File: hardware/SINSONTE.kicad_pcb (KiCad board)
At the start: 2 copper layers, 90 x 70 mm, 39 parts, among them J1 BAT, J10 Conn_01x01_Male, J11 Conn_01x01_Male, J12 Conn_01x04_Male, J13 Conn_01x01_Male, J14 Conn_01x02_Male, J2 CLOCK, J3 LIGHT_SENSOR, J4 Conn_01x20_Male, J5 Conn_01x01_Male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

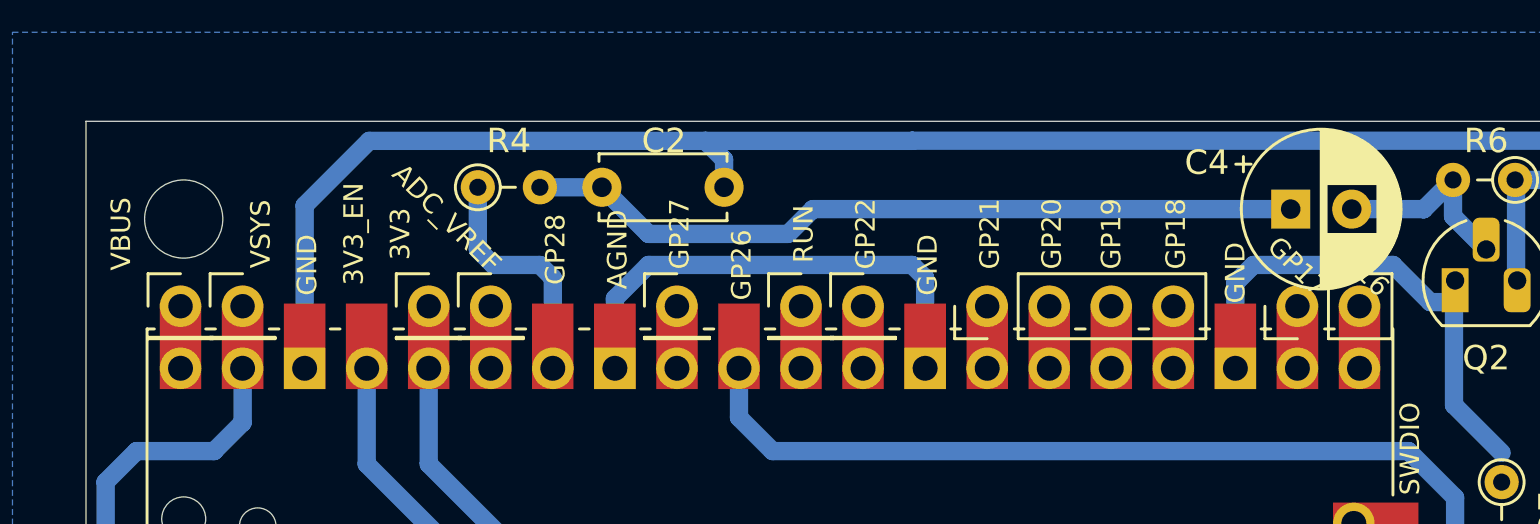
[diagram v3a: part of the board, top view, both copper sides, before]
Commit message: rpi second half conn aded all pins connector
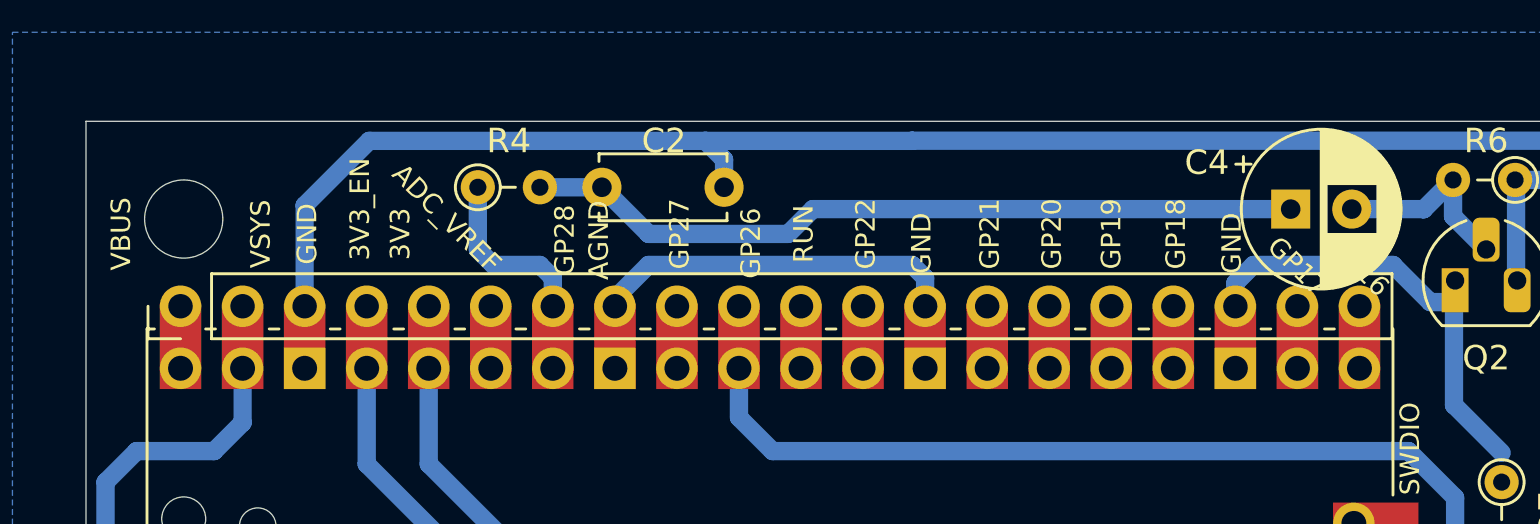
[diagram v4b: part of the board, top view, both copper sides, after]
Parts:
- removed J10, J11, J13, J6, J7, J8: Conn_01x01_Male, Connector_PinHeader_2.54mm:PinHeader_1x01_P2.54mm_Vertical
- removed J12: Conn_01x04_Male, Connector_PinHeader_2.54mm:PinHeader_1x04_P2.54mm_Vertical
- removed J14: Conn_01x02_Male, Connector_PinHeader_2.54mm:PinHeader_1x02_P2.54mm_Vertical
- J5: value Conn_01x01_Male -> Conn_01x20_Male; footprint Connector_PinHeader_2.54mm:PinHeader_1x01_P2.54mm_Vertical -> Connector_PinHeader_2.54mm:PinHeader_1x20_P2.54mm_Vertical
- moved J5 2.54 mm to (53.9, 57.6), turned to 90 degrees
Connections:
- J5 pad 1: Net-(BT1-Pad1) -> Net-(J5-Pad1)
- Q1 pad 3: Net-(Q1-Pad3) -> Net-(J5-Pad4)
- R4 pad 1: Net-(R4-Pad1) -> Net-(J5-Pad7)
- U1 pad 21: Net-(J14-Pad2) -> Net-(J5-Pad20)
- U1 pad 22: Net-(J14-Pad1) -> Net-(J5-Pad19)
- U1 pad 24: Net-(J12-Pad4) -> Net-(J5-Pad17)
- U1 pad 25: Net-(J12-Pad3) -> Net-(J5-Pad16)
- U1 pad 26: Net-(J12-Pad2) -> Net-(J5-Pad15)
- U1 pad 27: Net-(J12-Pad1) -> Net-(J5-Pad14)
- U1 pad 29: Net-(J11-Pad1) -> Net-(J5-Pad12)
- U1 pad 30: Net-(J8-Pad1) -> Net-(J5-Pad11)
- U1 pad 32: Net-(J7-Pad1) -> Net-(J5-Pad9)
- U1 pad 34: Net-(R4-Pad1) -> Net-(J5-Pad7)
- U1 pad 35: Net-(J10-Pad1) -> Net-(J5-Pad6)
- U1 pad 37: Net-(Q1-Pad3) -> Net-(J5-Pad4)
- U1 pad 40: Net-(J13-Pad1) -> Net-(J5-Pad1)
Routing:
- net Net-(J5-Pad4): track 0.00 -> 129.9 mm
- net Net-(Q1-Pad3): track 127.4 -> 0.00 mm
- net Net-(R4-Pad1): track 9.80 -> 0.00 mm
- net Net-(J5-Pad7): track 0.00 -> 9.80 mm
- net Net-(J8-Pad1): track 2.54 -> 0.00 mm
- net Net-(J7-Pad1): track 2.54 -> 0.00 mm
- net Net-(J5-Pad9): track 0.00 -> 2.54 mm
- net Net-(J5-Pad6): track 0.00 -> 2.54 mm
- net Net-(J5-Pad20): track 0.00 -> 2.54 mm
- net Net-(J5-Pad19): track 0.00 -> 2.54 mm
- net Net-(J5-Pad17): track 0.00 -> 2.54 mm
- net Net-(J5-Pad16): track 0.00 -> 2.54 mm
- net Net-(J5-Pad15): track 0.00 -> 2.54 mm
- net Net-(J5-Pad14): track 0.00 -> 2.54 mm
- net Net-(J5-Pad12): track 0.00 -> 2.54 mm
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
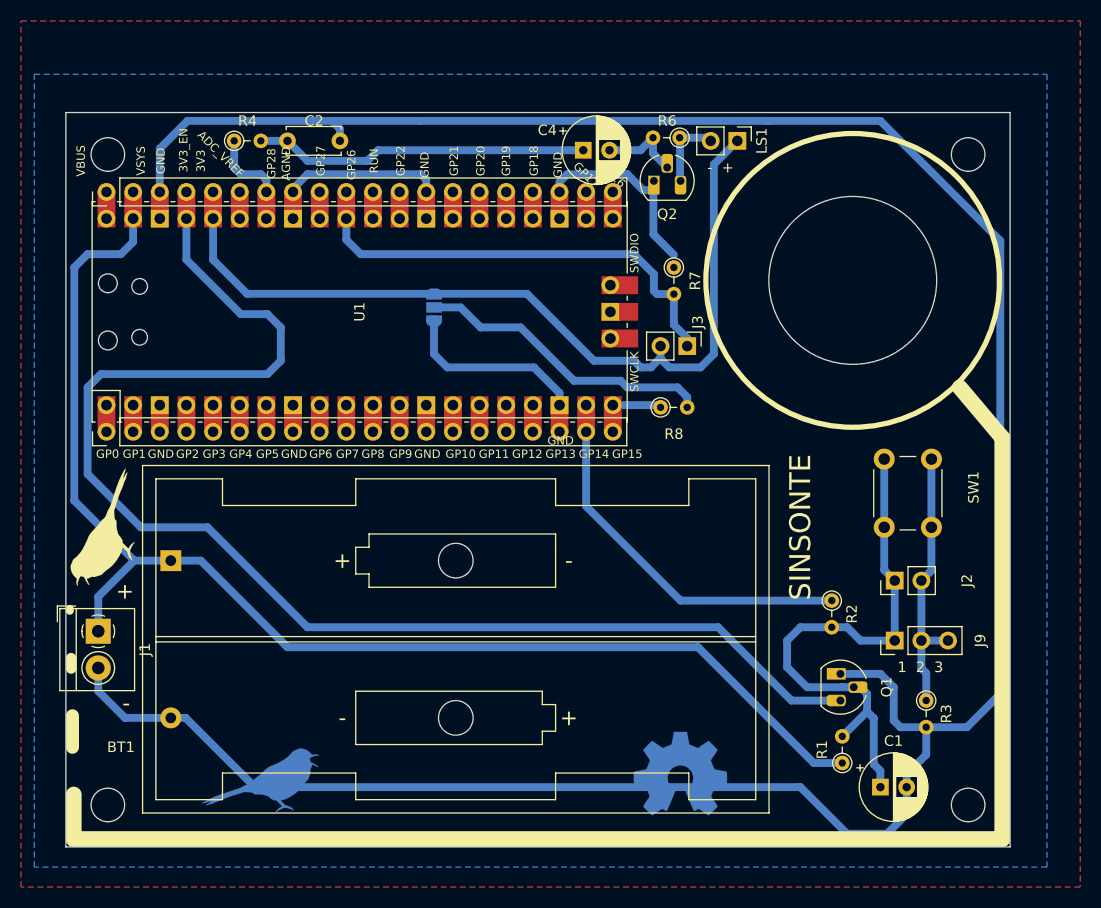
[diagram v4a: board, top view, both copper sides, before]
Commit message: added proto area
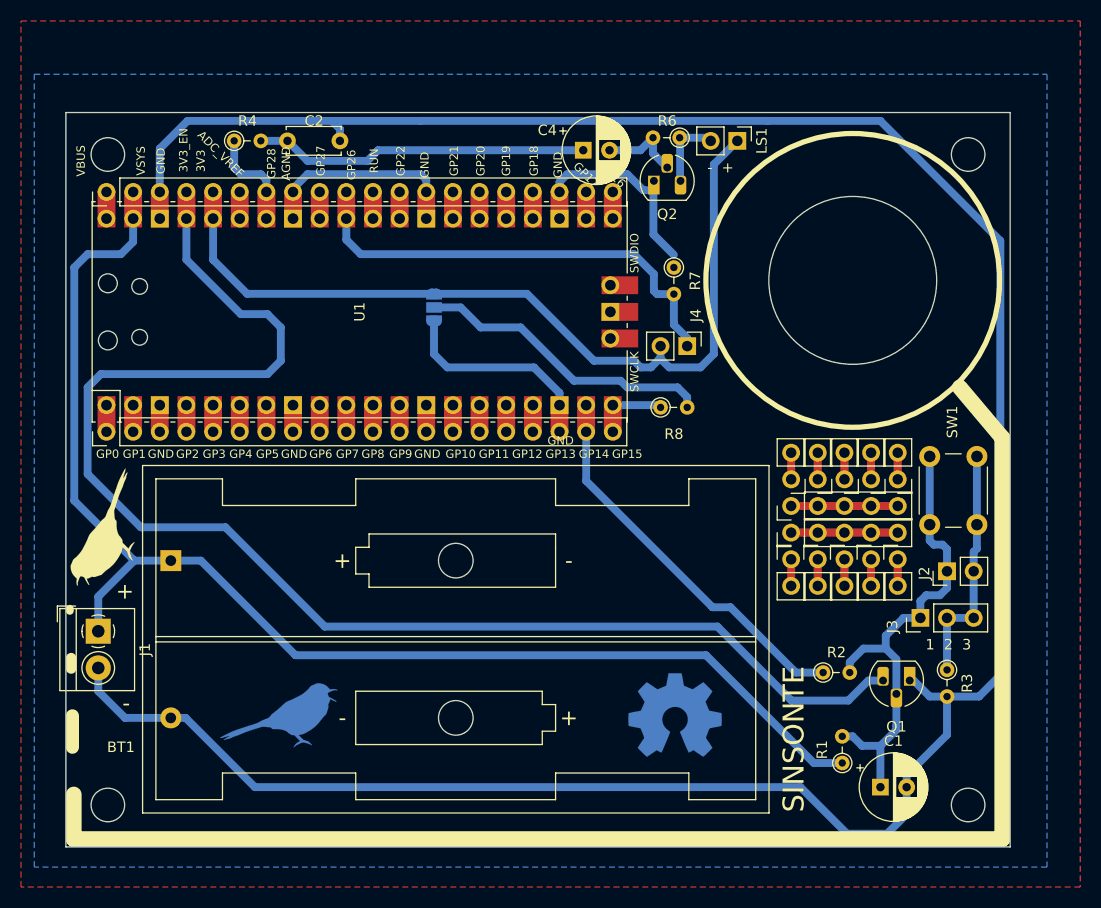
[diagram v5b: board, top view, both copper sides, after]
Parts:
- added J10: Conn_01x02_Male, Connector_PinHeader_2.54mm:PinHeader_1x02_P2.54mm_Vertical, F.Cu at (126.7, 92.6)
- added J11: Conn_01x02_Male, Connector_PinHeader_2.54mm:PinHeader_1x02_P2.54mm_Vertical, F.Cu at (124.2, 92.6)
- added J12: Conn_01x02_Male, Connector_PinHeader_2.54mm:PinHeader_1x02_P2.54mm_Vertical, F.Cu at (121.7, 92.6)
- added J13: Conn_01x02_Male, Connector_PinHeader_2.54mm:PinHeader_1x02_P2.54mm_Vertical, F.Cu at (119.1, 92.6)
- added J14: Conn_01x02_Male, Connector_PinHeader_2.54mm:PinHeader_1x02_P2.54mm_Vertical, F.Cu at (129.3, 85.0)
- added J15: Conn_01x02_Male, Connector_PinHeader_2.54mm:PinHeader_1x02_P2.54mm_Vertical, F.Cu at (126.7, 85.0)
- added J16: Conn_01x02_Male, Connector_PinHeader_2.54mm:PinHeader_1x02_P2.54mm_Vertical, F.Cu at (124.2, 85.0)
- added J17: Conn_01x02_Male, Connector_PinHeader_2.54mm:PinHeader_1x02_P2.54mm_Vertical, F.Cu at (121.7, 85.0)
- added J18: Conn_01x02_Male, Connector_PinHeader_2.54mm:PinHeader_1x02_P2.54mm_Vertical, F.Cu at (119.1, 85.0)
- added J7: Conn_01x05_Male, Connector_PinHeader_2.54mm:PinHeader_1x05_P2.54mm_Vertical, F.Cu at (119.1, 90.0)
- added J8: Conn_01x05_Male, Connector_PinHeader_2.54mm:PinHeader_1x05_P2.54mm_Vertical, F.Cu at (119.1, 87.5)
- added J9: Conn_01x02_Male, Connector_PinHeader_2.54mm:PinHeader_1x02_P2.54mm_Vertical, F.Cu at (129.3, 92.6)
- moved R2 6.91 mm to (122.2, 103.4), turned to 0 degrees
- moved Q1 6.63 mm to (130.4, 104.1), turned to 180 degrees
- moved G*** 6.45 mm to (70.3, 107.4)
- moved REF** 5.61 mm to (108.1, 107.4)
- moved J2 5.06 mm to (134.0, 93.7)
- moved SW1 4.34 mm to (132.3, 89.3)
- moved R3 3.53 mm to (134.0, 103.1)
- moved J3 3.26 mm to (131.4, 98.2)
- moved G*** 2.33 mm to (112.9, 79.5)
- renumbered J9 to J3, J3 to J4, J4 to J5, J5 to J6
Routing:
- net Net-(J8-Pad1): track 0.00 -> 20.3 mm
- net Net-(J7-Pad1): track 0.00 -> 20.3 mm
- net Net-(BT1-Pad2): track 323.3 -> 315.0 mm
- net Net-(C1-Pad1): track 53.0 -> 46.8 mm
- net Net-(J9-Pad1): track 0.00 -> 5.08 mm
- net Net-(J13-Pad1): track 0.00 -> 5.08 mm
- net Net-(J12-Pad1): track 0.00 -> 5.08 mm
- net Net-(J11-Pad1): track 0.00 -> 5.08 mm
- net Net-(J10-Pad1): track 0.00 -> 5.08 mm
- net Net-(J18-Pad1): track 0.00 -> 5.08 mm
- net Net-(J17-Pad1): track 0.00 -> 5.08 mm
- net Net-(J16-Pad1): track 0.00 -> 5.08 mm
- net Net-(J15-Pad1): track 0.00 -> 5.08 mm
- net Net-(J14-Pad1): track 0.00 -> 5.08 mm
- net Net-(J6-Pad4): track 129.9 -> 134.6 mm
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
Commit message: minor adjustments
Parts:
- moved J3 0.64 mm to (131.5, 98.8)
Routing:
- net Net-(J6-Pad4): track 134.6 -> 135.1 mm
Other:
- board text added: "MODEL A"
- board text removed: "V1"
